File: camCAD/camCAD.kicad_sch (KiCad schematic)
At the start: 0 parts

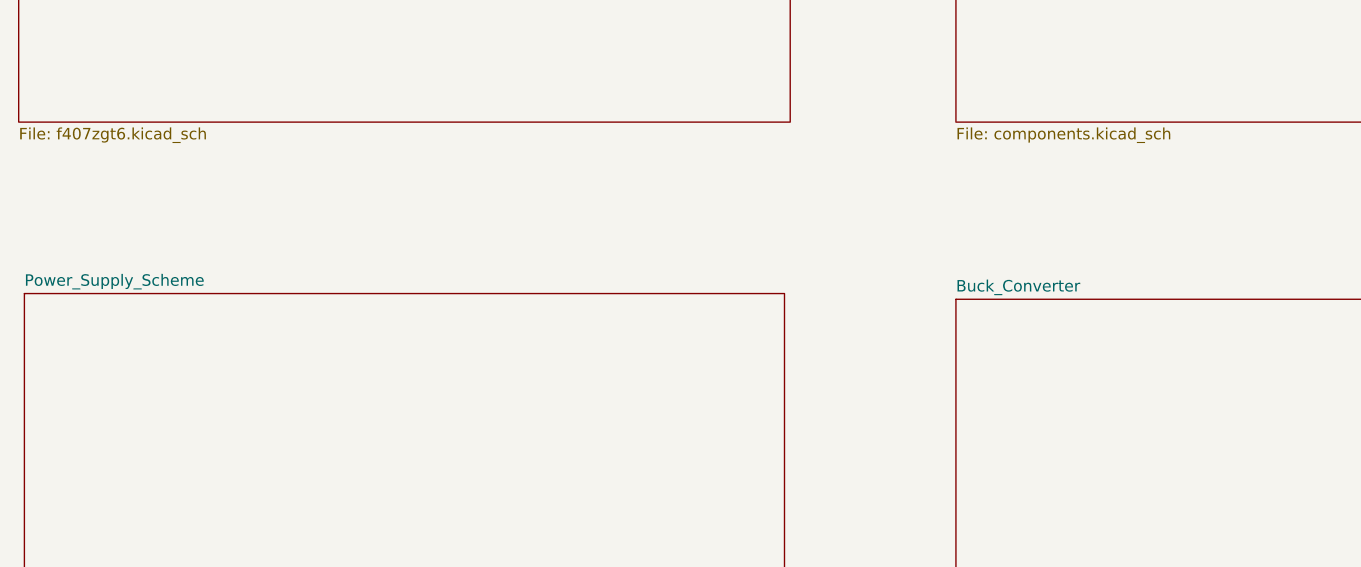
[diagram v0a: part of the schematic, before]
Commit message: Adding charging functionality
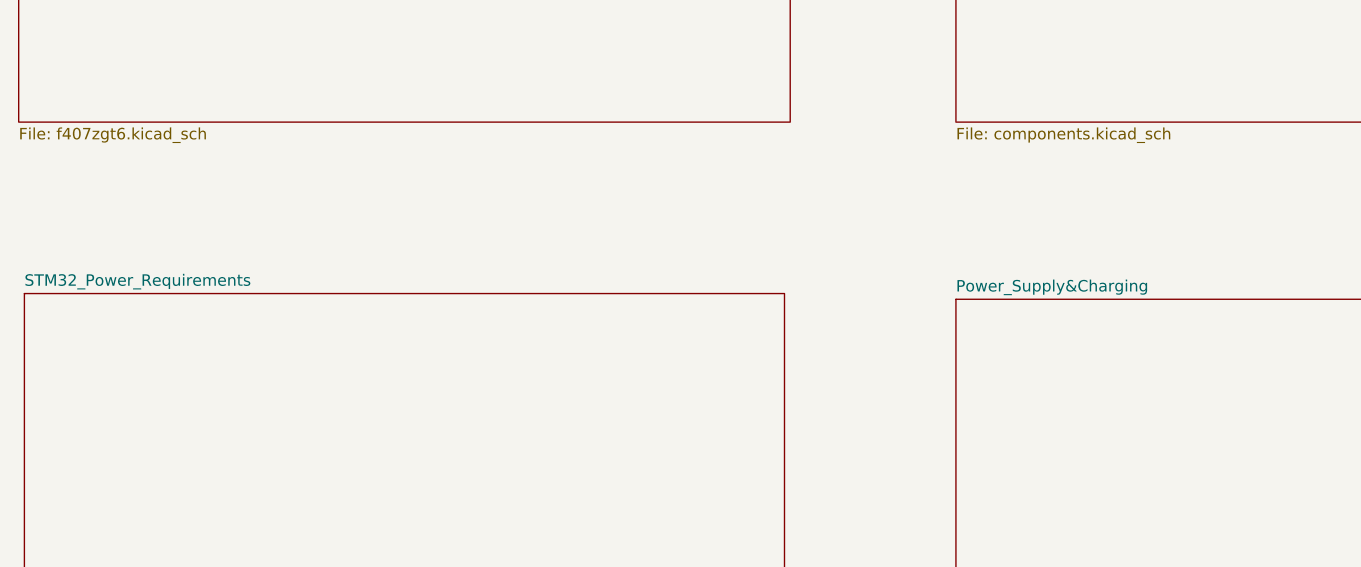
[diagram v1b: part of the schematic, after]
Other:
- sheet Buck_Converter renamed Power_Supply&Charging
- sheet Power_Supply_Scheme renamed STM32_Power_Requirements
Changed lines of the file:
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@@
 			(color 0 0 0 0)
 		)
-		(property "Sheetname" "Buck_Converter"
+		(property "Sheetname" "Power_Supply&Charging"
 			(at 129.54 149.1484 0)
 			(show_name no)
@@
 			(color 0 0 0 0)
 		)
-		(property "Sheetname" "Power_Supply_Scheme"
+		(property "Sheetname" "STM32_Power_Requirements"
 			(at 26.035 148.5134 0)
 			(show_name no)
